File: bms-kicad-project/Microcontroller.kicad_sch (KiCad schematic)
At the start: 40 parts, among them J4 Conn_02x18_Odd_Even, J5 Conn_02x18_Odd_Even, Q7 BSS308PE_H6327, SW1 KMR223G LFG, SW2 KMR223G LFG

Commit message: feat: put filtering and balancing circuits into hierarchical format
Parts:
- gave numbers to parts that had none: 29
- renumbered C25 to C6, C26 to C7, J4 to J3, J5 to J4, Q7 to Q1, R29 to R12, R32 to R8, R33 to R9, SW2 to SW1, SW1 to SW2
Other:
- company: (none) -> AeroNU - FixedWing

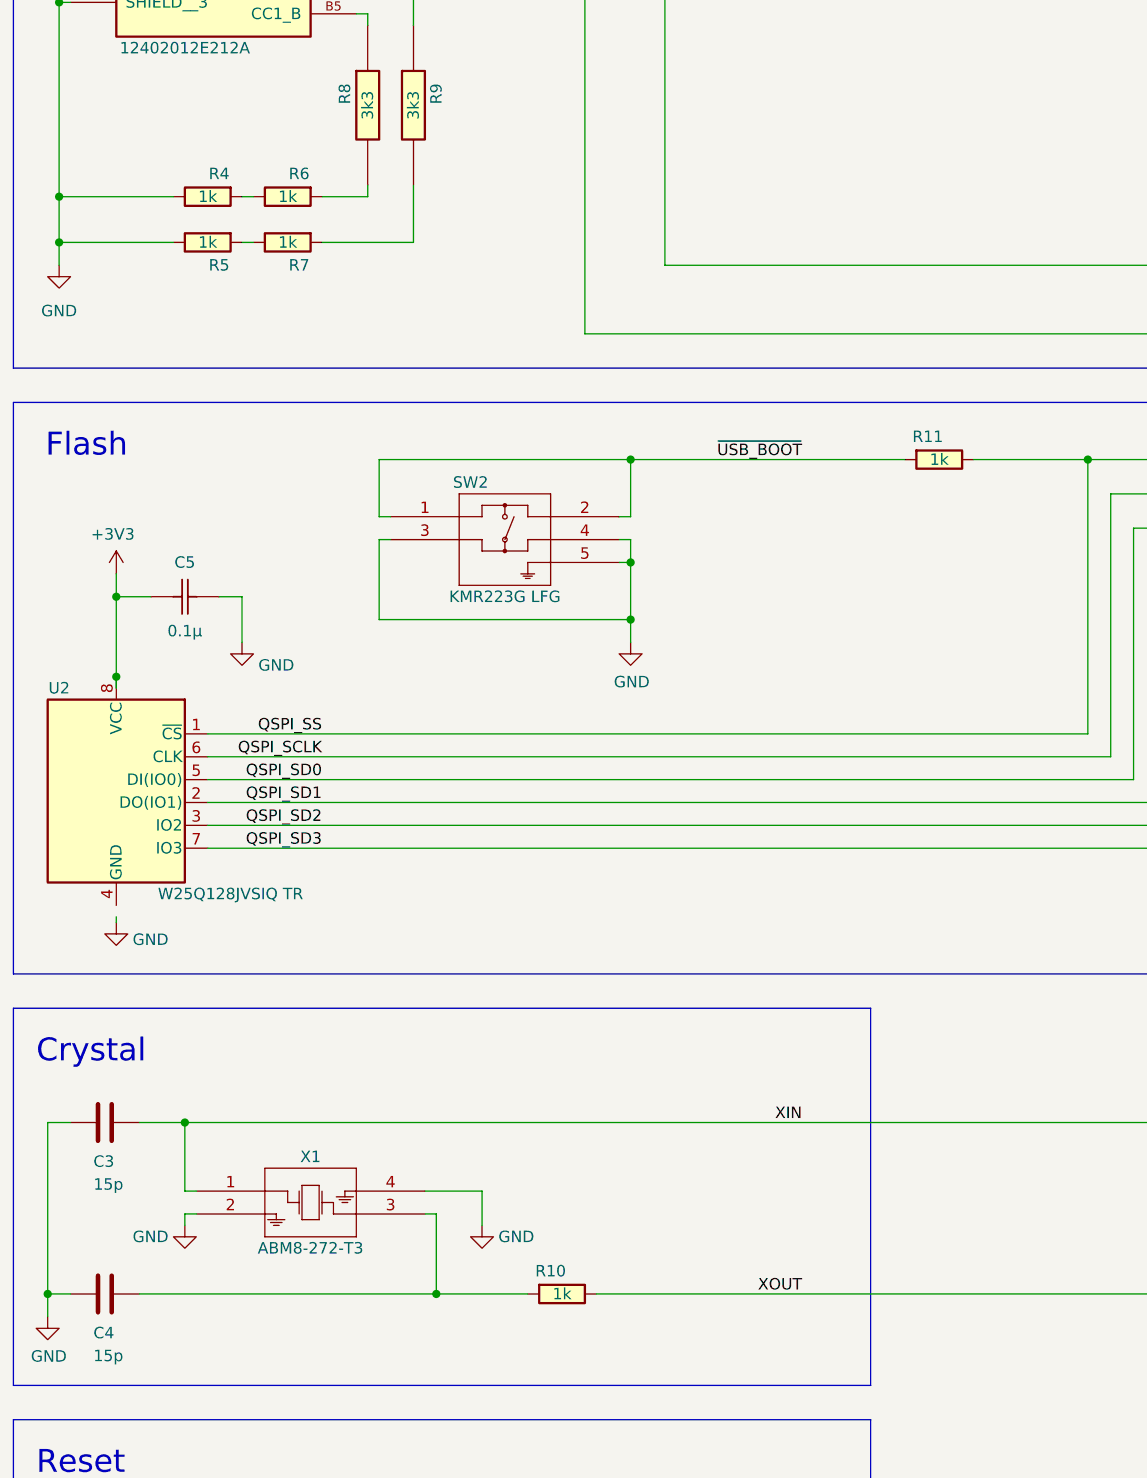
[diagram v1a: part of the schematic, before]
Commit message: feat: Added more to 5V Regulator Schematic
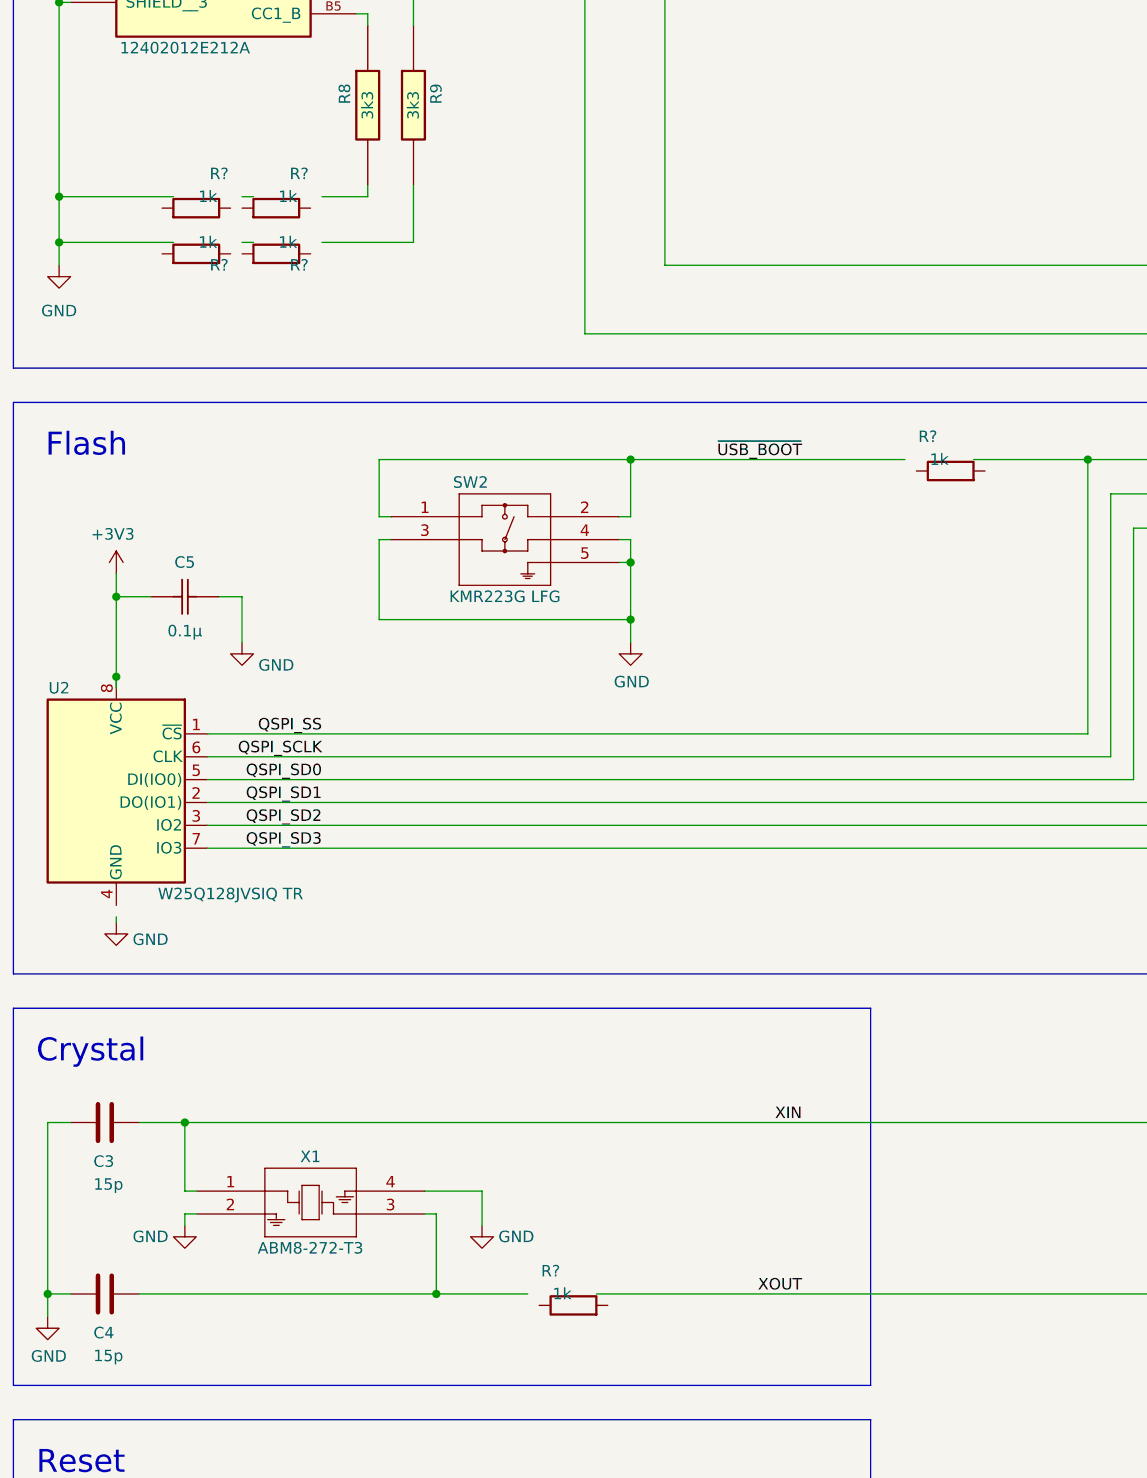
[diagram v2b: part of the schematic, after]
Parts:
- renumbered R11 to R?, R5 to R?, R4 to R?, R10 to R?, R7 to R?, R6 to R?
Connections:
- net GND: no longer R?.2, R?.2
- net QSPI_SS: no longer R?.2
- net XOUT: no longer R?.2
- net ~{USB_BOOT}: no longer R?.1
- net at R9.2: no longer R?.1
- net at C4.2, X1.3: no longer R?.1
- net at R?.1: no longer R?.2 (x2)
- net at R8.2: no longer R?.1
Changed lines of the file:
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@@
   (symbol (lib_id "FixedWing:RC0805FR-071KL") (at 115.57 123.19 0) (unit 1)
     (in_bom yes) (on_board yes) (dnp no)
-    (property "Reference" "R11" (at 116.84 119.38 0)
+    (property "Reference" "R?" (at 116.84 119.38 0)
       (effects (font (size 1.27 1.27)))
     )
@@
       (project "bms-board"
         (path "/8a7831d1-a913-4f04-8780-225d2234b41d/449bb263-23d7-4f07-b4f7-6cd2e161d267"
-          (reference "R11") (unit 1)
+          (reference "R?") (unit 1)
         )
       )
@@
   (symbol (lib_id "FixedWing:RC0805FR-071KL") (at 39.37 99.06 0) (mirror y) (unit 1)
     (in_bom yes) (on_board yes) (dnp no)
-    (property "Reference" "R5" (at 38.1 100.33 0)
+    (property "Reference" "R?" (at 38.1 100.33 0)
       (effects (font (size 1.27 1.27)))
     )
@@
       (project "bms-board"
         (path "/8a7831d1-a913-4f04-8780-225d2234b41d/449bb263-23d7-4f07-b4f7-6cd2e161d267"
-          (reference "R5") (unit 1)
+          (reference "R?") (unit 1)
         )
       )
@@
   (symbol (lib_id "FixedWing:RC0805FR-071KL") (at 39.37 93.98 0) (mirror y) (unit 1)
     (in_bom yes) (on_board yes) (dnp no)
-    (property "Reference" "R4" (at 38.1 90.17 0)
+    (property "Reference" "R?" (at 38.1 90.17 0)
       (effects (font (size 1.27 1.27)))
     )
@@
       (project "bms-board"
         (path "/8a7831d1-a913-4f04-8780-225d2234b41d/449bb263-23d7-4f07-b4f7-6cd2e161d267"
-          (reference "R4") (unit 1)
+          (reference "R?") (unit 1)
         )
       )
@@
   (symbol (lib_id "FixedWing:RC0805FR-071KL") (at 73.66 215.9 0) (unit 1)
     (in_bom yes) (on_board yes) (dnp no)
-    (property "Reference" "R10" (at 74.93 212.09 0)
+    (property "Reference" "R?" (at 74.93 212.09 0)
       (effects (font (size 1.27 1.27)))
     )
@@
       (project "bms-board"
         (path "/8a7831d1-a913-4f04-8780-225d2234b41d/449bb263-23d7-4f07-b4f7-6cd2e161d267"
-          (reference "R10") (unit 1)
+          (reference "R?") (unit 1)
         )
       )
@@
   (symbol (lib_id "FixedWing:RC0805FR-071KL") (at 48.26 99.06 0) (mirror y) (unit 1)
     (in_bom yes) (on_board yes) (dnp no)
-    (property "Reference" "R7" (at 46.99 100.33 0)
+    (property "Reference" "R?" (at 46.99 100.33 0)
       (effects (font (size 1.27 1.27)))
     )
@@
       (project "bms-board"
         (path "/8a7831d1-a913-4f04-8780-225d2234b41d/449bb263-23d7-4f07-b4f7-6cd2e161d267"
-          (reference "R7") (unit 1)
+          (reference "R?") (unit 1)
         )
       )
@@
   (symbol (lib_id "FixedWing:RC0805FR-071KL") (at 48.26 93.98 0) (mirror y) (unit 1)
     (in_bom yes) (on_board yes) (dnp no)
-    (property "Reference" "R6" (at 46.99 90.17 0)
+    (property "Reference" "R?" (at 46.99 90.17 0)
       (effects (font (size 1.27 1.27)))
     )
@@
       (project "bms-board"
         (path "/8a7831d1-a913-4f04-8780-225d2234b41d/449bb263-23d7-4f07-b4f7-6cd2e161d267"
-          (reference "R6") (unit 1)
-        )
-      )
+          (reference "R?") (unit 1)
+        )
+      )

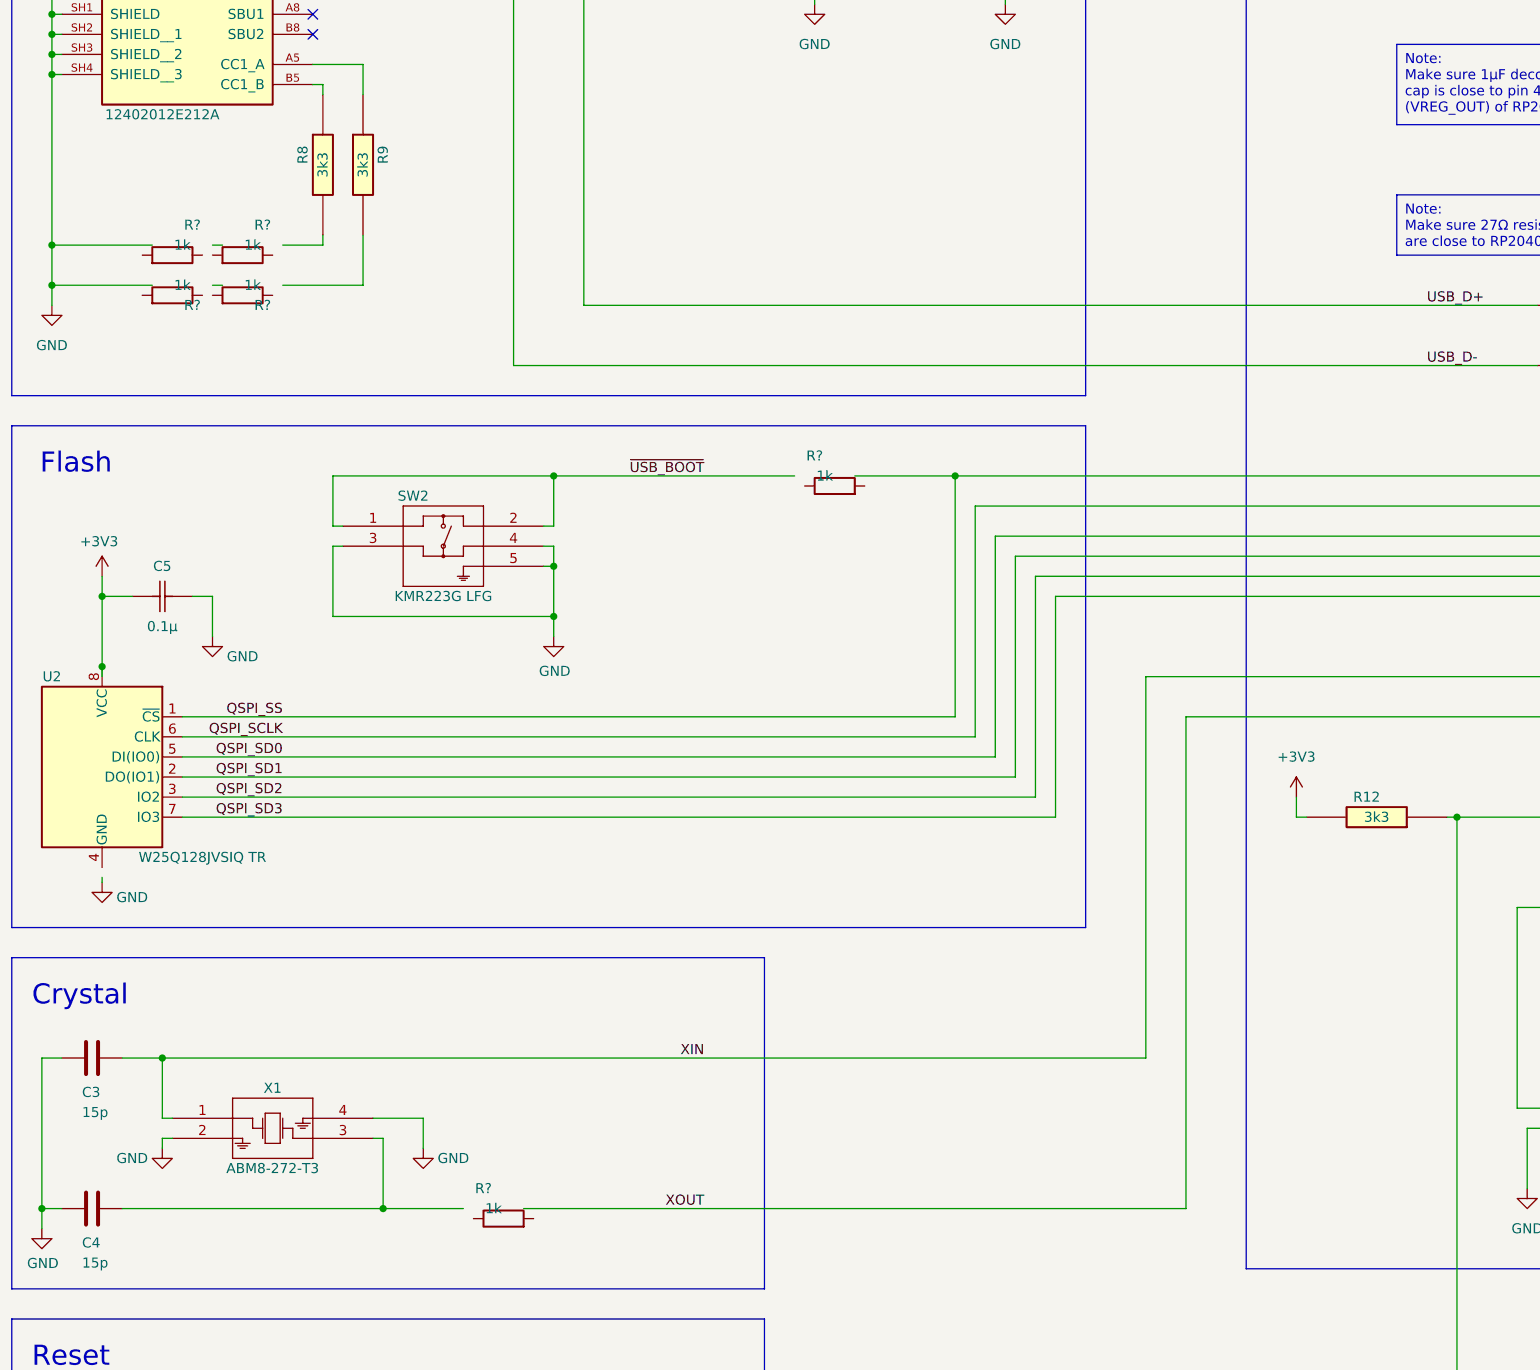
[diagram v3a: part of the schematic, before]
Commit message: feat: Added comment boxes and fixed 5V Regulator Schematic.
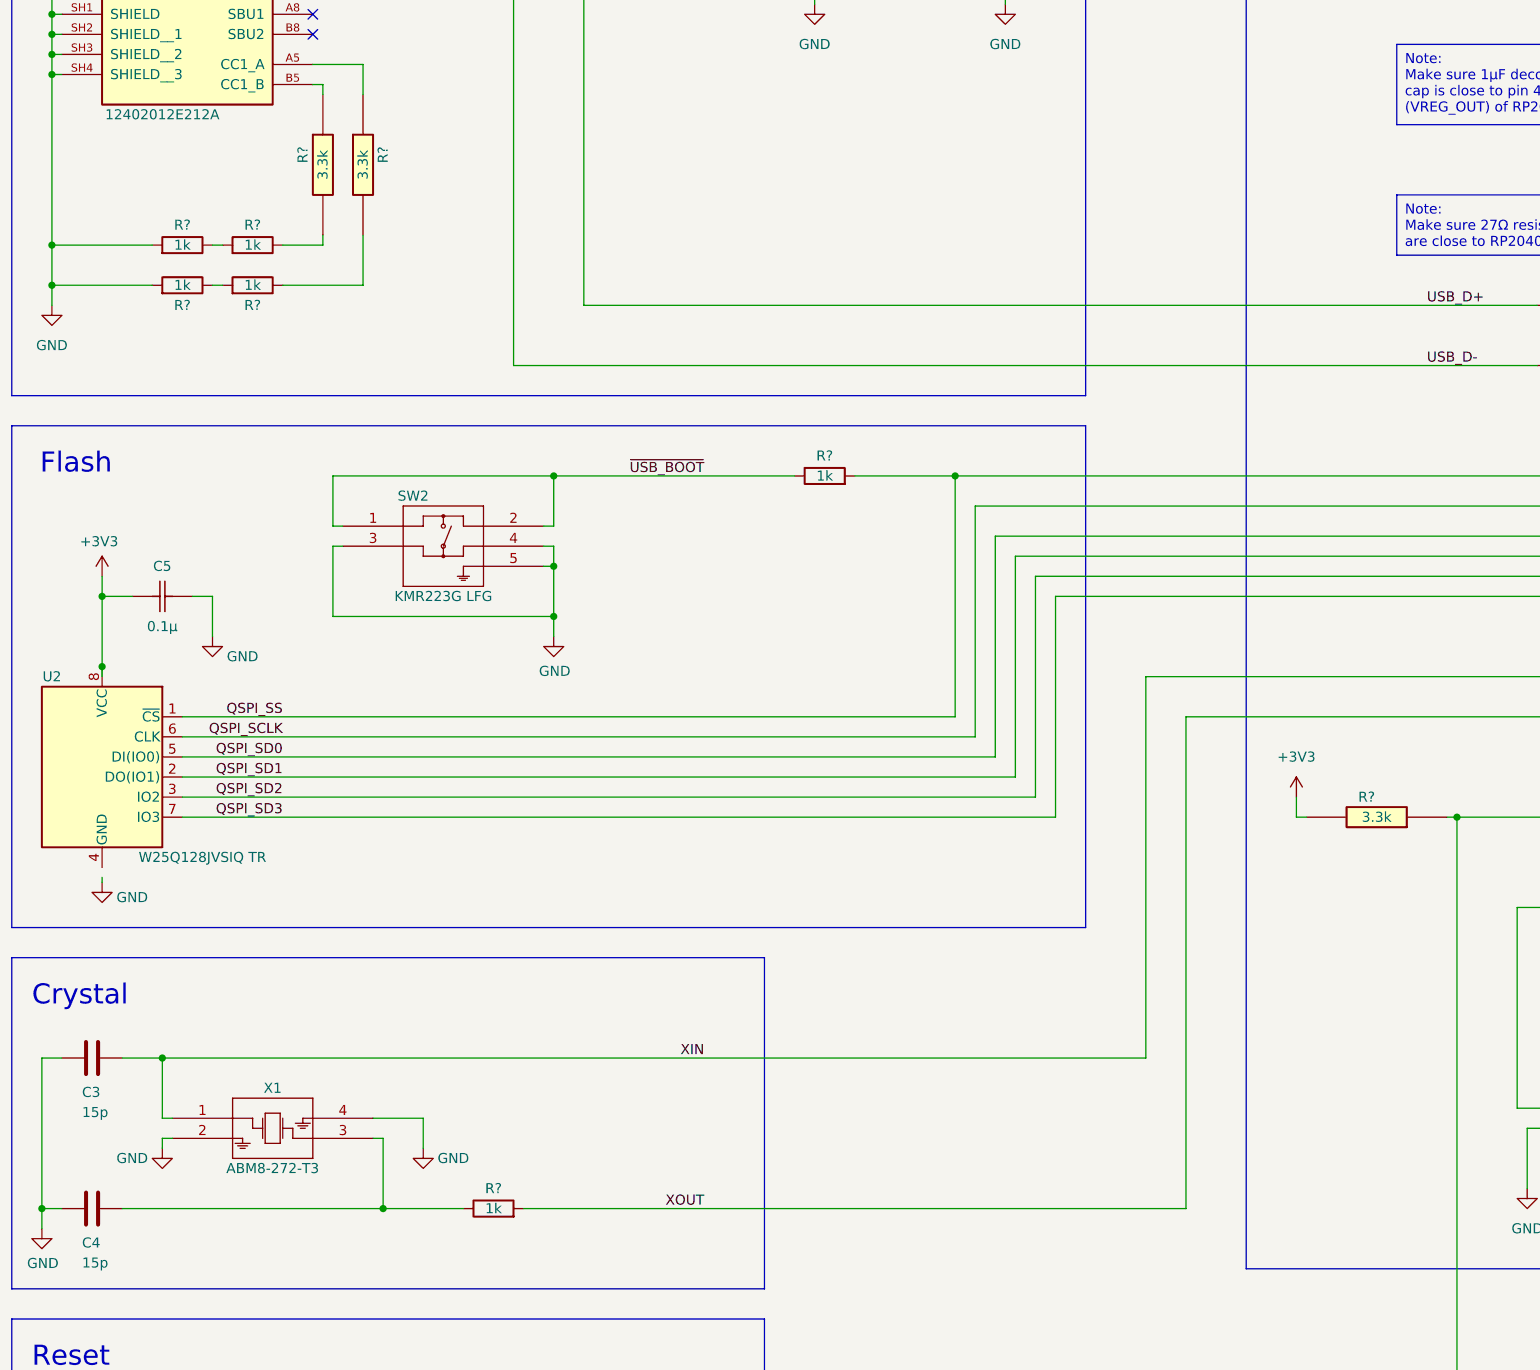
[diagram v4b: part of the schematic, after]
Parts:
- R?: renamed from R9; value 3k3 -> 3.3k
- R?: renamed from R12; value 3k3 -> 3.3k
- R?: renamed from R8; value 3k3 -> 3.3k
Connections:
- net GND: now also R?.2, R?.2
- net QSPI_SS: now also R?.2
- net XOUT: now also R?.2
- net ~{USB_BOOT}: now also R?.1
- net at R?.2: now also R?.1 (x2)
- net at C4.2, X1.3: now also R?.1
- net at R?.1: now also R?.2 (x2)
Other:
- moved on the sheet: R?
